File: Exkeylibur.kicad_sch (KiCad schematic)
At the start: 46 parts, among them SW1 SW_Push, SW10 SW_Push, SW11 SW_Push, SW12 SW_Push, SW13 SW_Push, SW14 SW_Push, SW15 SW_Push, SW16 SW_Push, SW17 SW_Push, SW18 SW_Push, SW2 SW_Push, SW22 SW_Push, SW23 SW_Push, SW24 SW_Push, SW25 SW_Push, SW26 SW_Push, SW27 SW_Push, SW28 SW_Push, SW29 SW_Push, SW3 SW_Push, SW30 SW_Push, SW31 SW_Push, SW32 SW_Push, SW33 SW_Push, SW34 SW_Push, SW35 SW_Push, SW36 SW_Push, SW37 SW_Push, SW38 SW_Push, SW39 SW_Push, SW4 SW_Push, SW5 SW_Push, SW6 SW_Push, SW7 SW_Push, SW8 SW_Push, SW9 SW_Push, U1 ProMicro, U2 ProMicro

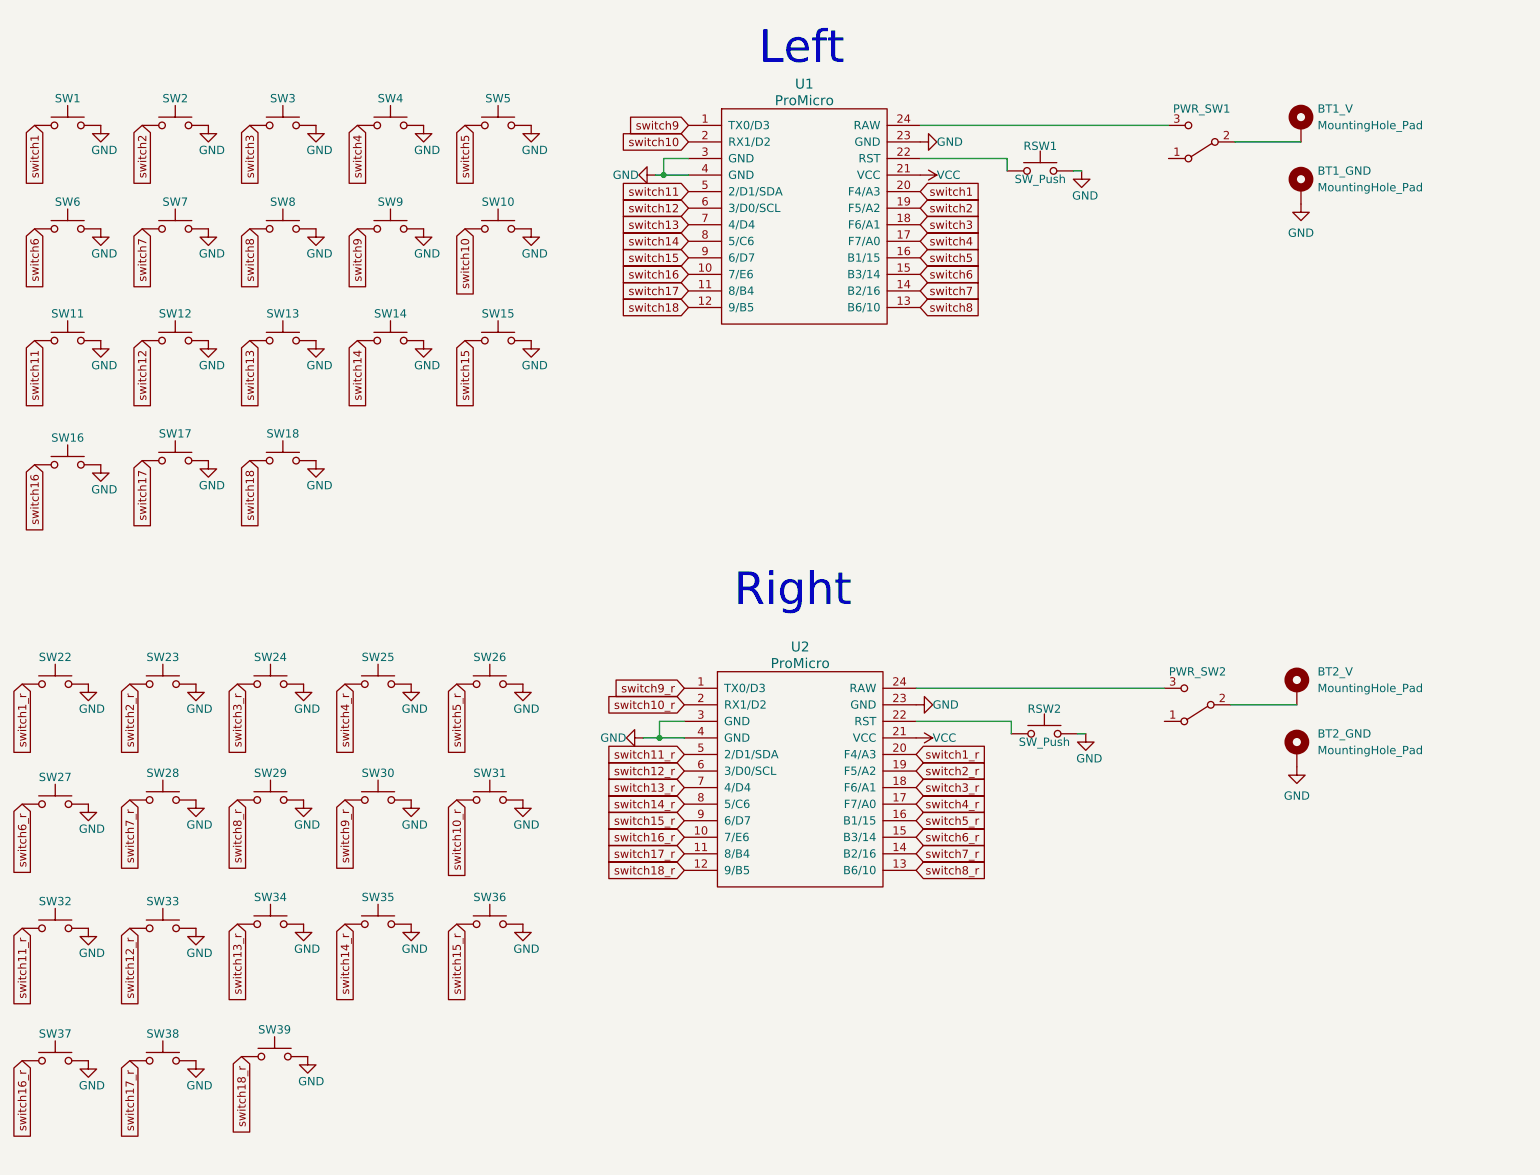
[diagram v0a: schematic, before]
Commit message: pcb reversible layout
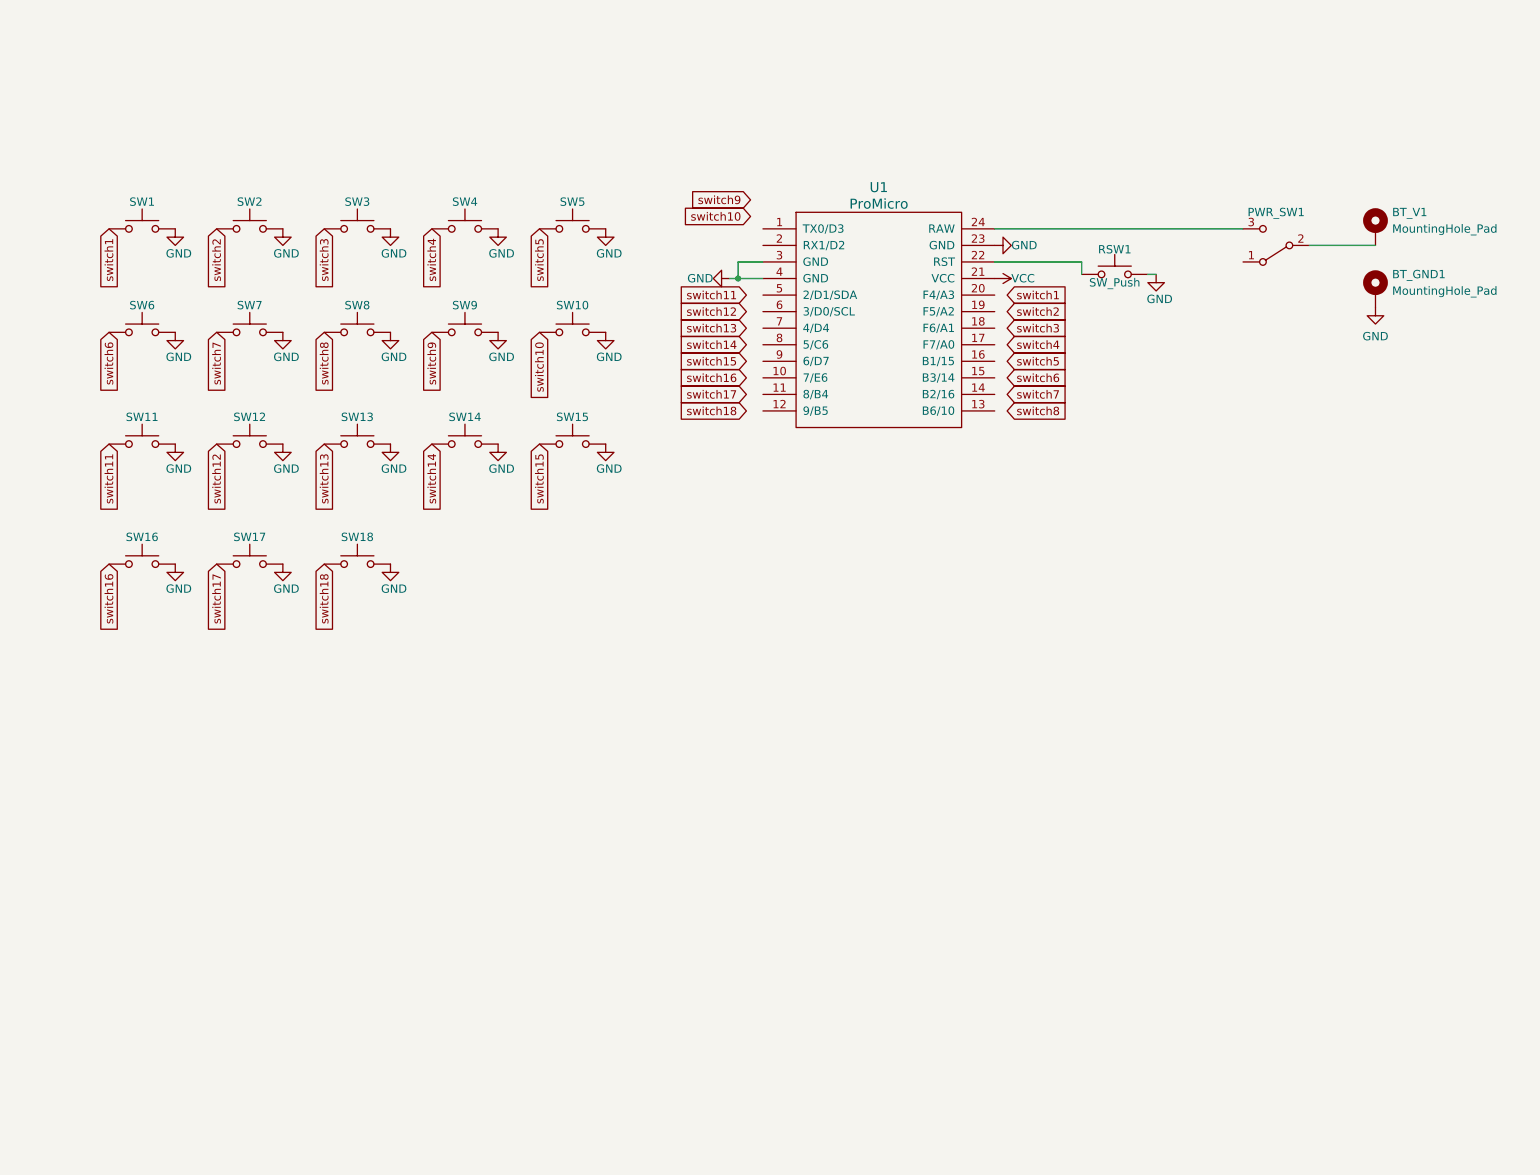
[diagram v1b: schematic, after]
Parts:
- removed BT2_GND, BT2_V: MountingHole_Pad, symbol Mechanical:MountingHole_Pad
- removed PWR_SW2: SW_SPDT, symbol Switch:SW_SPDT
- removed RSW2, SW22, SW23, SW24, SW25, SW26, SW27, SW28, SW29, SW30, SW31, SW32, SW33, SW34, SW35, SW36, SW37, SW38, SW39: SW_Push, symbol Switch:SW_Push
- removed U2: ProMicro, symbol Exkeylibur:ProMicro
- PWR_SW1: footprint (none) -> Exkeylibur:keyboard_power_switch
- RSW1: footprint (none) -> Exkeylibur:reset_switch
- SW1: footprint (none) -> Exkeylibur:choc_switch_reversible
- U1: footprint (none) -> Exkeylibur:ProMicro_v3_min
- renumbered BT1_GND to BT_GND1, BT1_V to BT_V1
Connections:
- net switch1: no longer U1.20 (F4/A3)
- net switch10: no longer U1.2 (RX1/D2)
- net switch11: no longer U1.5 (2/D1/SDA)
- net switch12: no longer U1.6 (3/D0/SCL)
- net switch13: no longer U1.7 (4/D4)
- net switch14: no longer U1.8 (5/C6)
- net switch15: no longer U1.9 (6/D7)
- net switch16: no longer U1.10 (7/E6)
- net switch17: no longer U1.11 (8/B4)
- net switch18: no longer U1.12 (9/B5)
- net switch2: no longer U1.19 (F5/A2)
- net switch3: no longer U1.18 (F6/A1)
- net switch4: no longer U1.17 (F7/A0)
- net switch5: no longer U1.16 (B1/15)
- net switch6: no longer U1.15 (B3/14)
- net switch7: no longer U1.14 (B2/16)
- net switch8: no longer U1.13 (B6/10)
- net switch9: no longer U1.1 (TX0/D3)
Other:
- note removed: "Left"
- note removed: "Right"
- moved on the sheet: BT_GND1, BT_V1, PWR_SW1, RSW1, SW1, SW10, SW11, SW12, SW13, SW14, SW15, SW16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

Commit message: backannotate to schematic:
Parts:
- BT_GND1: footprint (none) -> Exkeylibur:bat_gnd_mountingHole
- BT_V1: footprint (none) -> Exkeylibur:Bat_MountingHole
- PWR_SW1: footprint Exkeylibur:keyboard_power_switch -> Kailh:SPDT_C128955
- SW10, SW11, SW12, SW13, SW14, SW15, SW16, SW17, SW18, SW2, SW3, SW4, SW5, SW6, SW7, SW8, SW9: footprint (none) -> Exkeylibur:choc_switch_reversible
- U1: footprint Exkeylibur:ProMicro_v3_min -> kbd:ProMicro_v3_min
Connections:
- net switch1: now also U1.12 (9/B5)
- net switch10: now also U1.15 (B3/14)
- net switch11: now also U1.16 (B1/15)
- net switch12: now also U1.17 (F7/A0)
- net switch13: now also U1.10 (7/E6)
- net switch14: now also U1.9 (6/D7)
- net switch15: now also U1.8 (5/C6)
- net switch16: now also U1.7 (4/D4)
- net switch17: now also U1.6 (3/D0/SCL)
- net switch18: now also U1.5 (2/D1/SDA)
- net switch2: now also U1.18 (F6/A1)
- net switch3: now also U1.19 (F5/A2)
- net switch4: now also U1.20 (F4/A3)
- net switch5: now also U1.2 (RX1/D2)
- net switch6: now also U1.1 (TX0/D3)
- net switch7: now also U1.11 (8/B4)
- net switch8: now also U1.13 (B6/10)
- net switch9: now also U1.14 (B2/16)
